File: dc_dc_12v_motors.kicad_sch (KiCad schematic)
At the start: 18 parts, among them Q7 CSD17505Q5A, Q8 CSD18540Q5B, U9 LM3150MH

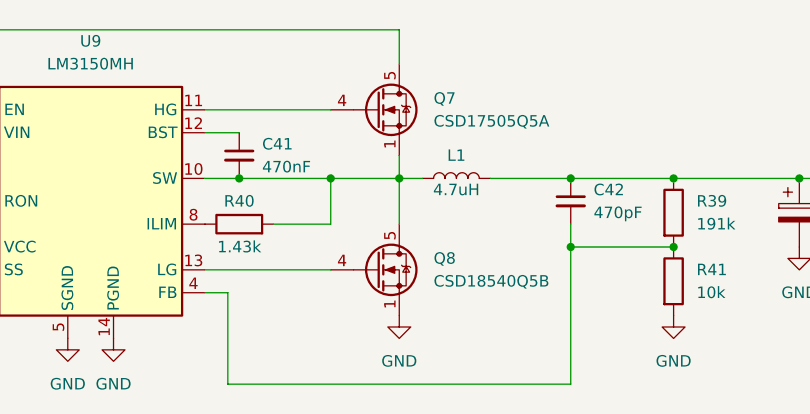
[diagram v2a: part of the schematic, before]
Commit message: updated to kicad 9, added comparator-based power source switching
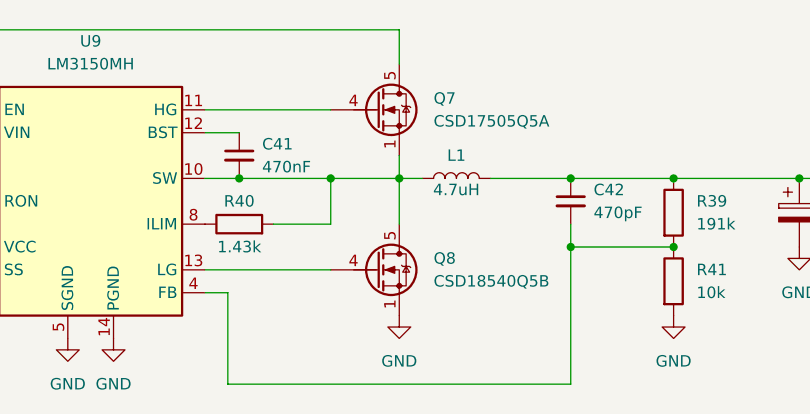
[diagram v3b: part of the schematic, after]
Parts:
- U9: footprint Package_SO:HTSSOP-14-1EP_4.4x5mm_P0.65mm_EP3.4x5mm_Mask3x3.1mm -> Package_SO:Texas_HTSSOP-14-1EP_4.4x5mm_P0.65mm_EP3.4x5mm_Mask3.155x3.255mm
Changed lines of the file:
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@@
 (kicad_sch
-	(version 20231120)
+	(version 20250114)
 	(generator "eeschema")
-	(generator_version "8.0")
+	(generator_version "9.0")
 	(paper "A4")
 	(title_block
@@
 		(shape output)
 		(at 248.92 91.44 0)
-		(fields_autoplaced yes)
 		(effects
 			(font
@@
 		(shape input)
 		(at 54.61 74.93 180)
-		(fields_autoplaced yes)
 		(effects
 			(font
@@
 			)
 		)
-		(property "Description" ""
+		(property "Description" "Power symbol creates a global label with name \"GND\" , ground"
 			(at 102.87 86.36 0)
 			(effects
@@
 			)
 		)
-		(property "Description" ""
+		(property "Description" "Power symbol creates a global label with name \"GND\" , ground"
 			(at 223.52 99.06 0)
 			(effects
@@
 			)
 		)
-		(property "Description" ""
+		(property "Description" "Power symbol creates a global label with name \"GND\" , ground"
 			(at 237.49 99.06 0)
 			(effects
@@
 			)
 		)
-		(property "Description" ""
+		(property "Description" "Power symbol creates a global label with name \"GND\" , ground"
 			(at 209.55 106.68 0)
 			(effects
@@
 			)
 		)
-		(property "Description" ""
+		(property "Description" "Power symbol creates a global label with name \"GND\" , ground"
 			(at 147.32 109.22 0)
 			(effects
@@
 			)
 		)
-		(property "Description" ""
+		(property "Description" "Power symbol creates a global label with name \"GND\" , ground"
 			(at 74.93 86.36 0)
 			(effects
@@
 			)
 		)
-		(property "Description" ""
+		(property "Description" "Power symbol creates a global label with name \"GND\" , ground"
 			(at 127 109.22 0)
 			(effects
@@
 			)
 		)
-		(property "Description" ""
+		(property "Description" "Power symbol creates a global label with name \"GND\" , ground"
 			(at 90.17 86.36 0)
 			(effects
@@
 			)
 		)
-		(property "Description" ""
+		(property "Description" "100A Id, 30V Vds, NexFET N-Channel Power MOSFET, 3.5mOhm Ron, 10nC Qg(typ), SON8 5x6mm"
 			(at 176.53 83.82 0)
 			(effects
@@
 			)
 		)
-		(property "Description" ""
+		(property "Description" "Special symbol for telling ERC where power comes from"
 			(at 246.38 91.44 0)
 			(effects
@@
 			)
 		)
-		(property "Footprint" "Package_SO:HTSSOP-14-1EP_4.4x5mm_P0.65mm_EP3.4x5mm_Mask3x3.1mm"
+		(property "Footprint" "Package_SO:Texas_HTSSOP-14-1EP_4.4x5mm_P0.65mm_EP3.4x5mm_Mask3.155x3.255mm"
 			(at 147.32 107.95 0)
 			(effects
@@
 			)
 		)
-		(property "Description" ""
+		(property "Description" "42V Wide Vin synchronous Buck controller, HTSSOP-14"
 			(at 144.78 93.98 0)
 			(effects
@@
 			)
 		)
-		(property "Description" ""
+		(property "Description" "Power symbol creates a global label with name \"GND\" , ground"
 			(at 142.24 109.22 0)
 			(effects
@@
 			)
 		)
-		(property "Description" ""
+		(property "Description" "100A Id, 60V Vds, NexFET N-Channel Power MOSFET, 2.2mOhm Ron, 41nC Qg(typ), SON8 5x6mm"
 			(at 176.53 101.6 0)
 			(effects
@@
 			)
 		)
-		(property "Description" ""
+		(property "Description" "Power symbol creates a global label with name \"GND\" , ground"
 			(at 111.76 106.68 0)
 			(effects
@@
 			)
 		)
-		(property "Description" ""
+		(property "Description" "Power symbol creates a global label with name \"GND\" , ground"
 			(at 60.96 86.36 0)
 			(effects
@@
 			)
 		)
-		(property "Description" ""
+		(property "Description" "Power symbol creates a global label with name \"GND\" , ground"
 			(at 179.07 106.68 0)
 			(effects
